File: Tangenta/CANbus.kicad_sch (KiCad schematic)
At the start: 1 part, among them J15 RC01133

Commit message: ...
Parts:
- removed J15: RC01133, RJ45_SIMPLE:RJ45_SIMPLE, symbol RJ45_SIMPLE:RC01133
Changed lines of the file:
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@@
 (kicad_sch (version 20230121) (generator eeschema)
   (paper "A4")
-  (symbol (lib_id "RJ45_SIMPLE:RC01133") (at 82.55 69.215 0) (unit 1)
-    (in_bom yes) (on_board yes) (dnp no) (fields_autoplaced)
-    (property "Reference" "J15" (at 81.28 52.07 0)
-      (effects (font (size 1.27 1.27)))
-    )
-    (property "Value" "RC01133" (at 81.28 54.61 0)
-      (effects (font (size 1.27 1.27)))
-    )
-    (property "Footprint" "RJ45_SIMPLE:RJ45_SIMPLE" (at 83.82 94.615 0)
-      (effects (font (size 1.27 1.27) italic) hide)
-    )
-    (property "Datasheet" "https://atta.szlcsc.com/upload/public/pdf/source/20200728/C708616_F79F0C1A8A5D9701E7B7144C9F29FA5C.pdf" (at 71.12 97.155 0)
-      (effects (font (size 1.27 1.27)) (justify left) hide)
-    )
-    (property "LCSC" "C708616" (at 76.2 92.075 0)
-      (effects (font (size 1.27 1.27)) hide)
-    )
-    (pin "1")
-    (pin "10")
-    (pin "2")
-    (pin "3")
-    (pin "4")
-    (pin "5")
-    (pin "6")
-    (pin "7")
-    (pin "8")
-    (pin "9")
-    (instances
-      (project "Tangenta"
-        (path "/358d1bcf-7599-4352-8c4d-baa18a5f09e6/b5394a48-5ef8-44c9-9d56-604d4ce6d7c8"
-          (reference "J15") (unit 1)
-        )
-      )
-    )
-  )
 )

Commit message: ...
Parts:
- added C178: 47uF, CAP_L5:CAP_L5, symbol CAP_L5:16CE47FSS
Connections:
- new net 5V: C178.1
- new net GNDREF: C178.2
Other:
- added sheet CAN_Channel_1 (CAN_Channel_1.kicad_sch)
- added sheet CAN_Channel_2 (CAN_Channel_2.kicad_sch)

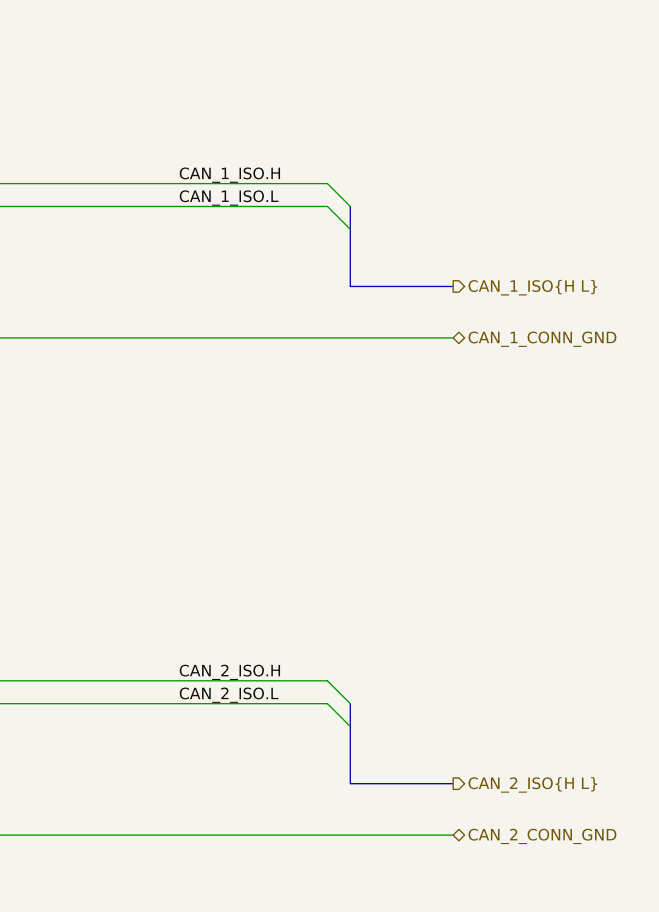
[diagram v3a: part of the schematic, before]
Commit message: CANbus done, UART terminals in progress...
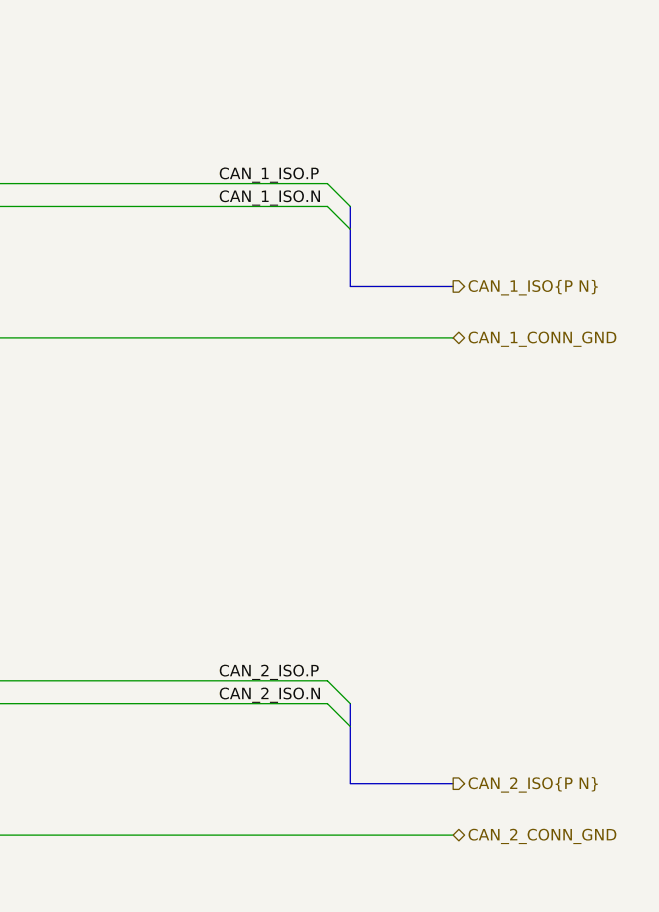
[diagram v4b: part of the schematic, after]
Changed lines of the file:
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@@
     (effects (font (size 1.27 1.27)) (justify right bottom))
   )
-  (label "CAN_1_ISO.H" (at 220.98 61.595 0) (fields_autoplaced)
+  (label "CAN_1_ISO.P" (at 225.425 61.595 0) (fields_autoplaced)
     (effects (font (size 1.27 1.27)) (justify left bottom))
   )
@@
     (effects (font (size 1.27 1.27)) (justify right bottom))
   )
-  (label "CAN_2_ISO.L" (at 220.98 119.38 0) (fields_autoplaced)
+  (label "CAN_2_ISO.N" (at 225.425 119.38 0) (fields_autoplaced)
     (effects (font (size 1.27 1.27)) (justify left bottom))
   )
-  (label "CAN_2_ISO.H" (at 220.98 116.84 0) (fields_autoplaced)
+  (label "CAN_2_ISO.P" (at 225.425 116.84 0) (fields_autoplaced)
     (effects (font (size 1.27 1.27)) (justify left bottom))
   )
-  (label "CAN_1_ISO.L" (at 220.98 64.135 0) (fields_autoplaced)
+  (label "CAN_1_ISO.N" (at 225.425 64.135 0) (fields_autoplaced)
     (effects (font (size 1.27 1.27)) (justify left bottom))
   )
@@
     (effects (font (size 1.27 1.27)) (justify right))
   )
-  (hierarchical_label "CAN_2_ISO{H L}" (shape output) (at 251.46 128.27 0) (fields_autoplaced)
+  (hierarchical_label "CAN_2_ISO{P N}" (shape output) (at 251.46 128.27 0) (fields_autoplaced)
     (effects (font (size 1.27 1.27)) (justify left))
   )
@@
     (effects (font (size 1.27 1.27)) (justify right))
   )
-  (hierarchical_label "CAN_1_ISO{H L}" (shape output) (at 251.46 73.025 0) (fields_autoplaced)
+  (hierarchical_label "CAN_1_ISO{P N}" (shape output) (at 251.46 73.025 0) (fields_autoplaced)
     (effects (font (size 1.27 1.27)) (justify left))
   )

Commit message: Libraries exported from global to project.
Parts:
- C178: symbol CAP_L5:16CE47FSS -> CholaSymbolsPrjLib:16CE47FSS
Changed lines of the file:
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@@
     (effects (font (size 1.27 1.27)) (justify left))
   )
-  (symbol (lib_id "CAP_L5:16CE47FSS") (at 46.99 36.83 0) (unit 1)
+  (symbol (lib_id "CholaSymbolsPrjLib:16CE47FSS") (at 46.99 36.83 0) (unit 1)
     (in_bom yes) (on_board yes) (dnp no)
     (property "Reference" "C178" (at 48.26 34.925 0)

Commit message: ...
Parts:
- C178: symbol CholaSymbolsPrjLib:16CE47FSS -> LocalPrjLib:16CE47FSS
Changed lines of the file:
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@@
     (effects (font (size 1.27 1.27)) (justify left))
   )
-  (symbol (lib_id "CholaSymbolsPrjLib:16CE47FSS") (at 46.99 36.83 0) (unit 1)
+  (symbol (lib_id "LocalPrjLib:16CE47FSS") (at 46.99 36.83 0) (unit 1)
     (in_bom yes) (on_board yes) (dnp no)
     (property "Reference" "C178" (at 48.26 34.925 0)

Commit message: Fixes, new approach.
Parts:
- C178: symbol LocalPrjLib:16CE47FSS -> LocalSymbolsPrjLib:16CE47FSS
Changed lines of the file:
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@@
     (effects (font (size 1.27 1.27)) (justify left))
   )
-  (symbol (lib_id "LocalPrjLib:16CE47FSS") (at 46.99 36.83 0) (unit 1)
+  (symbol (lib_id "LocalSymbolsPrjLib:16CE47FSS") (at 46.99 36.83 0) (unit 1)
     (in_bom yes) (on_board yes) (dnp no)
     (property "Reference" "C178" (at 48.26 34.925 0)
